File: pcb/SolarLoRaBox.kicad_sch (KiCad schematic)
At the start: 56 parts, among them J1 Conn_01x02_Socket, J2 Conn_01x02_Socket, J3 Conn_01x04_Socket, J4 Conn_ARM_SWD_TagConnect_TC2030, J5 Conn_01x04_Socket, J6 Conn_01x04_Socket, J7 Conn_01x04_Socket, J8 Conn_01x04_Socket, SW1 SSSS811101, SW2 SW_Push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

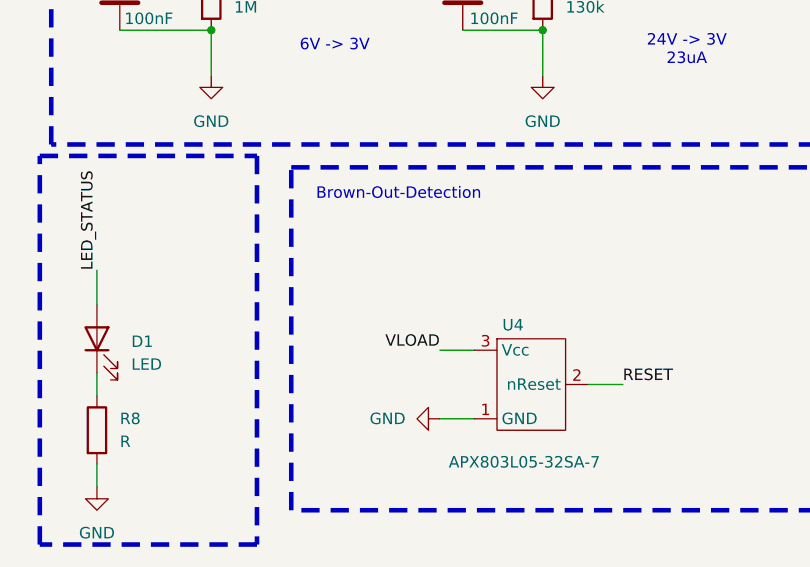
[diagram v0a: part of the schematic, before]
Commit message: pcb, sch: fix invalid uart rx/tx silk print, add C infront of reset ic
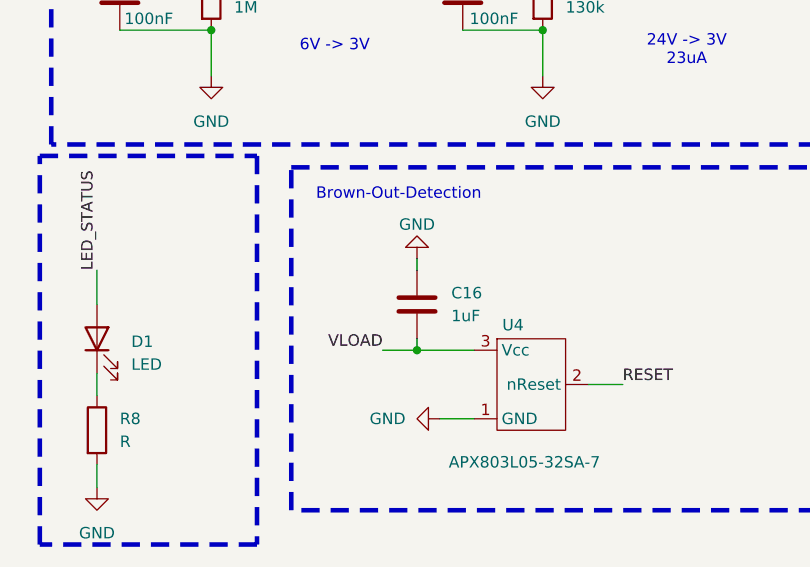
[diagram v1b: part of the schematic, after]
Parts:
- added C16: 1uF, Capacitor_SMD:C_0805_2012Metric_Pad1.18x1.45mm_HandSolder, symbol Device:C
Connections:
- net GND: now also C16.1
- net VLOAD: now also C16.2
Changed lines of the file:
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@@
 	)
 	(junction
+		(at 298.45 85.09)
+		(diameter 0)
+		(color 0 0 0 0)
+	)
+	(junction
 		(at 113.03 274.32)
 		(diameter 0)
@@
 	(wire
 		(pts
+			(xy 298.45 74.93) (xy 298.45 76.2)
+		)
+		(stroke
+			(width 0)
+			(type default)
+		)
+	)
+	(wire
+		(pts
 			(xy 162.56 285.75) (xy 172.72 285.75)
 		)
@@
 	(wire
 		(pts
+			(xy 298.45 83.82) (xy 298.45 85.09)
+		)
+		(stroke
+			(width 0)
+			(type default)
+		)
+	)
+	(wire
+		(pts
 			(xy 374.65 241.3) (xy 379.73 241.3)
 		)
@@
 	(wire
 		(pts
-			(xy 300.99 85.09) (xy 304.8 85.09)
+			(xy 294.64 85.09) (xy 298.45 85.09)
 		)
 		(stroke
@@
 	(wire
 		(pts
+			(xy 298.45 85.09) (xy 304.8 85.09)
+		)
+		(stroke
+			(width 0)
+			(type default)
+		)
+	)
+	(wire
+		(pts
 			(xy 152.4 151.13) (xy 152.4 154.94)
 		)
@@
 	)
 	(label "VLOAD"
-		(at 300.99 85.09 180)
+		(at 294.64 85.09 180)
 		(fields_autoplaced yes)
 		(effects
@@
 	)
 	(symbol
+		(lib_id "power:GND")
+		(at 298.45 74.93 180)
+		(unit 1)
+		(exclude_from_sim no)
+		(in_bom yes)
+		(on_board yes)
+		(dnp no)
+		(property "Reference" "#PWR029"
+			(at 298.45 68.58 0)
+			(effects
+				(font
+					(size 1.27 1.27)
+				)
+				(hide yes)
+			)
+		)
+		(property "Value" "GND"
+			(at 298.45 71.12 0)
+			(effects
+				(font
+					(size 1.27 1.27)
+				)
+			)
+		)
+		(property "Footprint" ""
+			(at 298.45 74.93 0)
+			(effects
+				(font
+					(size 1.27 1.27)
+				)
+				(hide yes)
+			)
+		)
+		(property "Datasheet" ""
+			(at 298.45 74.93 0)
+			(effects
+				(font
+					(size 1.27 1.27)
+				)
+				(hide yes)
+			)
+		)
+		(property "Description" "Power symbol creates a global label with name \"GND\" , ground"
+			(at 298.45 74.93 0)
+			(effects
+				(font
+					(size 1.27 1.27)
+				)
+				(hide yes)
+			)
+		)
+		(pin "1"
+		)
+		(instances
+			(project ""
+				(path "/256f162e-4f54-42b3-a315-b65231ce36a5"
+					(reference "#PWR029")
+					(unit 1)
+				)
+			)
+		)
+	)
+	(symbol
 		(lib_id "Connector:Conn_01x04_Socket")
 		(at 118.11 143.51 90)
@@
 					(unit 1)
 				)
+			)
+		)
+	)
+	(symbol
+		(lib_id "Device:C")
+		(at 298.45 80.01 0)
+		(unit 1)
+		(exclude_from_sim no)
+		(in_bom yes)
+		(on_board yes)
+		(dnp no)
+		(fields_autoplaced yes)
+		(property "Reference" "C16"
+			(at 302.26 78.7399 0)
+			(effects
+				(font
+					(size 1.27 1.27)
+				)
+				(justify left)
+			)
+		)
+		(property "Value" "1uF"
+			(at 302.26 81.2799 0)
+			(effects
+				(font
+					(size 1.27 1.27)
+				)
+				(justify left)
+			)
+		)
+		(property "Footprint" "Capacitor_SMD:C_0805_2012Metric_Pad1.18x1.45mm_HandSolder"
+			(at 299.4152 83.82 0)
+			(effects
+				(font
+					(size 1.27 1.27)
+				)
+				(hide yes)
+			)
+		)
+		(property "Datasheet" "~"
+			(at 298.45 80.01 0)
+			(effects
+				(font
+					(size 1.27 1.27)
+				)
+				(hide yes)
+			)
+		)
+		(property "Description" "Unpolarized capacitor"
+			(at 298.45 80.01 0)
+			(effects
+				(font
+					(size 1.27 1.27)
+				)
+				(hide yes)
+			)
+		)
+		(pin "1"
+		)
+		(pin "2"
+		)
+		(instances
+			(project ""
+				(path "/256f162e-4f54-42b3-a315-b65231ce36a5"
+					(reference "C16")
+					(unit 1)
+				)

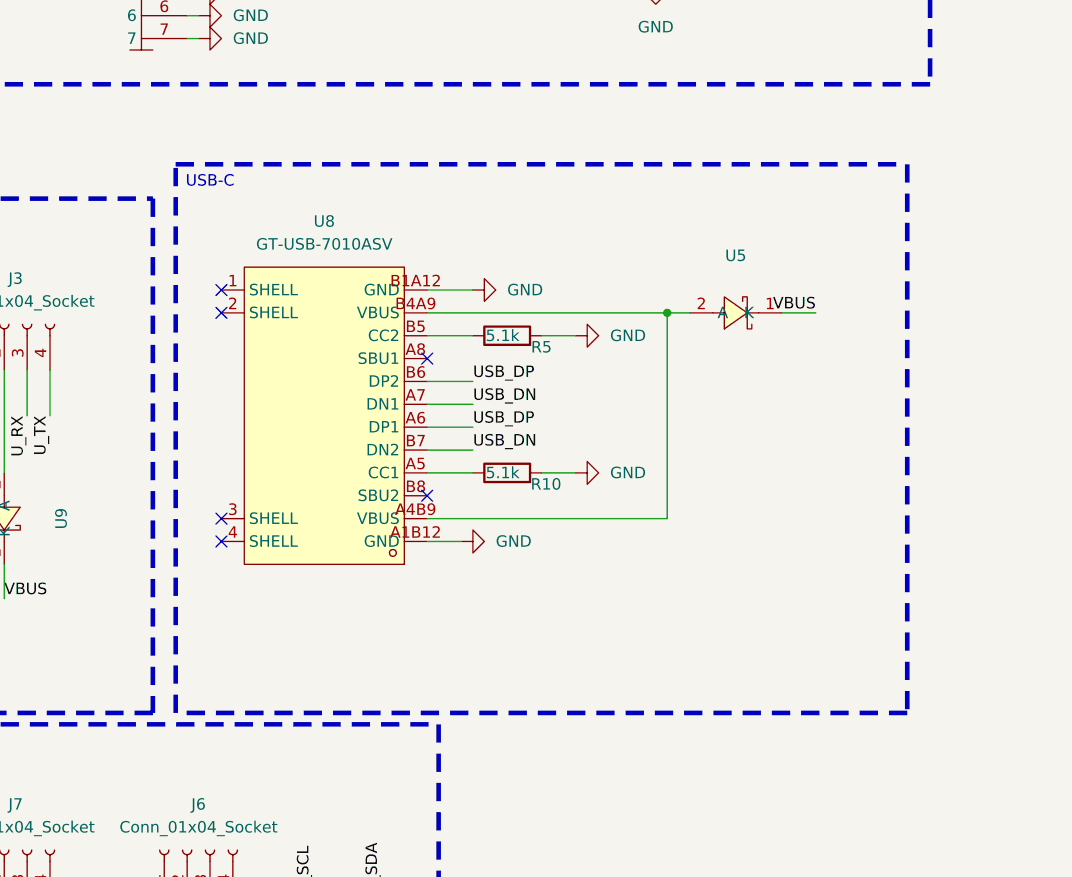
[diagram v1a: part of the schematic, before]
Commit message: pcb, sch, doc: lots of cosmetic fixes
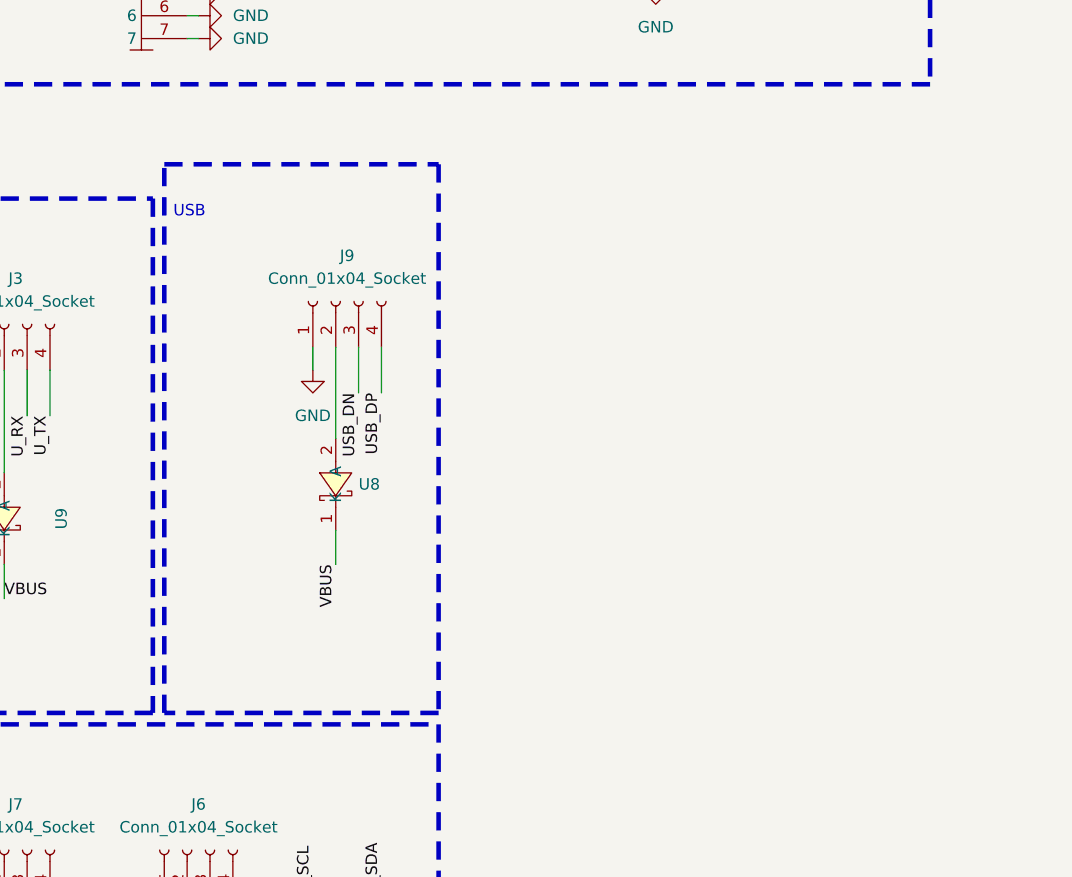
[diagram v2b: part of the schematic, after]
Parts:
- removed R10, R5: 5.1k, Resistor_SMD:R_0805_2012Metric_Pad1.20x1.40mm_HandSolder, symbol Device:R
- removed U5: SS26_C5350986, footprints:SMA_L4.3-W2.6-LS5.1-RD, symbol own_symbols:SS26_C5350986
- removed U8: GT-USB-7010ASV, footprints:USB-C-SMD_G-SWITCH_GT-USB-7010ASV, symbol own_symbols:GT-USB-7010ASV
- added J9: Conn_01x04_Socket, Connector_JST:JST_PH_B4B-PH-K_1x04_P2.00mm_Vertical, symbol Connector:Conn_01x04_Socket
- added U8: SS26_C5350986, footprints:SMA_L4.3-W2.6-LS5.1-RD, symbol own_symbols:SS26_C5350986
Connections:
- net GND: now also J9.1 (Pin_1)
- net USB_DN: now also J9.3 (Pin_3)
- net USB_DP: now also J9.4 (Pin_4)
- net VBUS: now also U8.1 (K)
- new net: J9.2 (Pin_2), U8.2 (A)
- no-connect marks 23 -> 17
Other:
- note added: "USB"
- note removed: "USB-C"

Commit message: pcb, sch: switch MISO/MOSI on Windbond flash as they are inverted!
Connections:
- net FLASH_MISO: now also U6.2 (DO(IO1)); no longer U6.5 (DI(IO0))
- net FLASH_MOSI: now also U6.5 (DI(IO0)); no longer U6.2 (DO(IO1))
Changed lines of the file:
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@@
 		)
 	)
-	(label "FLASH_MOSI"
+	(label "FLASH_MISO"
 		(at 360.68 123.19 180)
 		(fields_autoplaced yes)
@@
 		)
 	)
-	(label "FLASH_MISO"
+	(label "FLASH_MOSI"
 		(at 360.68 120.65 180)
 		(fields_autoplaced yes)

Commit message: EVALUATION: ADC verified
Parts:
- added H1: MountingHole, MountingHole:MountingHole_4.3mm_M4_DIN965, symbol Mechanical:MountingHole
- added J10: Conn_01x05_Socket, Connector_JST:JST_PH_B5B-PH-K_1x05_P2.00mm_Vertical, symbol Connector:Conn_01x05_Socket
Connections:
- net GND: now also J10.1 (Pin_1)
- net GPIO1: now reaches U2.40 (PB4)
- net GPIO1: now also J10.5 (Pin_5)
- net GPIO2: now reaches U2.41 (PB5)
- net GPIO2: now also J10.4 (Pin_4)
- net GPIO3: now reaches U2.42 (PB6)
- net GPIO3: now also J10.3 (Pin_3)
- net GPIO4: now reaches U2.43 (PB7)
- net GPIO4: now also J10.2 (Pin_2)
- no-connect marks 17 -> 13
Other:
- note added: "GPIO"

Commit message: pcb, sch: match silk print and schematic
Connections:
- net GPIO1 renamed GPIOD
- net GPIO2 renamed GPIOC
- net GPIO3 renamed GPIOB
- net GPIO4 renamed GPIOA
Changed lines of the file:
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@@
 		)
 	)
-	(label "GPIO3"
+	(label "GPIOB"
 		(at 468.63 259.08 0)
 		(effects
@@
 		)
 	)
-	(label "GPIO2"
+	(label "GPIOC"
 		(at 182.88 152.4 270)
 		(effects
@@
 		)
 	)
-	(label "GPIO2"
+	(label "GPIOC"
 		(at 468.63 256.54 0)
 		(effects
@@
 		)
 	)
-	(label "GPIO1"
+	(label "GPIOD"
 		(at 468.63 254 0)
 		(effects
@@
 		)
 	)
-	(label "GPIO3"
+	(label "GPIOB"
 		(at 180.34 152.4 270)
 		(effects
@@
 		)
 	)
-	(label "GPIO4"
+	(label "GPIOA"
 		(at 177.8 152.4 270)
 		(effects
@@
 		)
 	)
-	(label "GPIO4"
+	(label "GPIOA"
 		(at 468.63 261.62 0)
 		(effects
@@
 		)
 	)
-	(label "GPIO1"
+	(label "GPIOD"
 		(at 185.42 152.4 270)
 		(effects
